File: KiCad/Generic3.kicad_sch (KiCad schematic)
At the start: 29 parts, among them J1 DC, J2 I/O, J3 USB-C, U1 ESP32-PICO-MINI-02, U2 LMR16006+FB, U3 FT231XQ

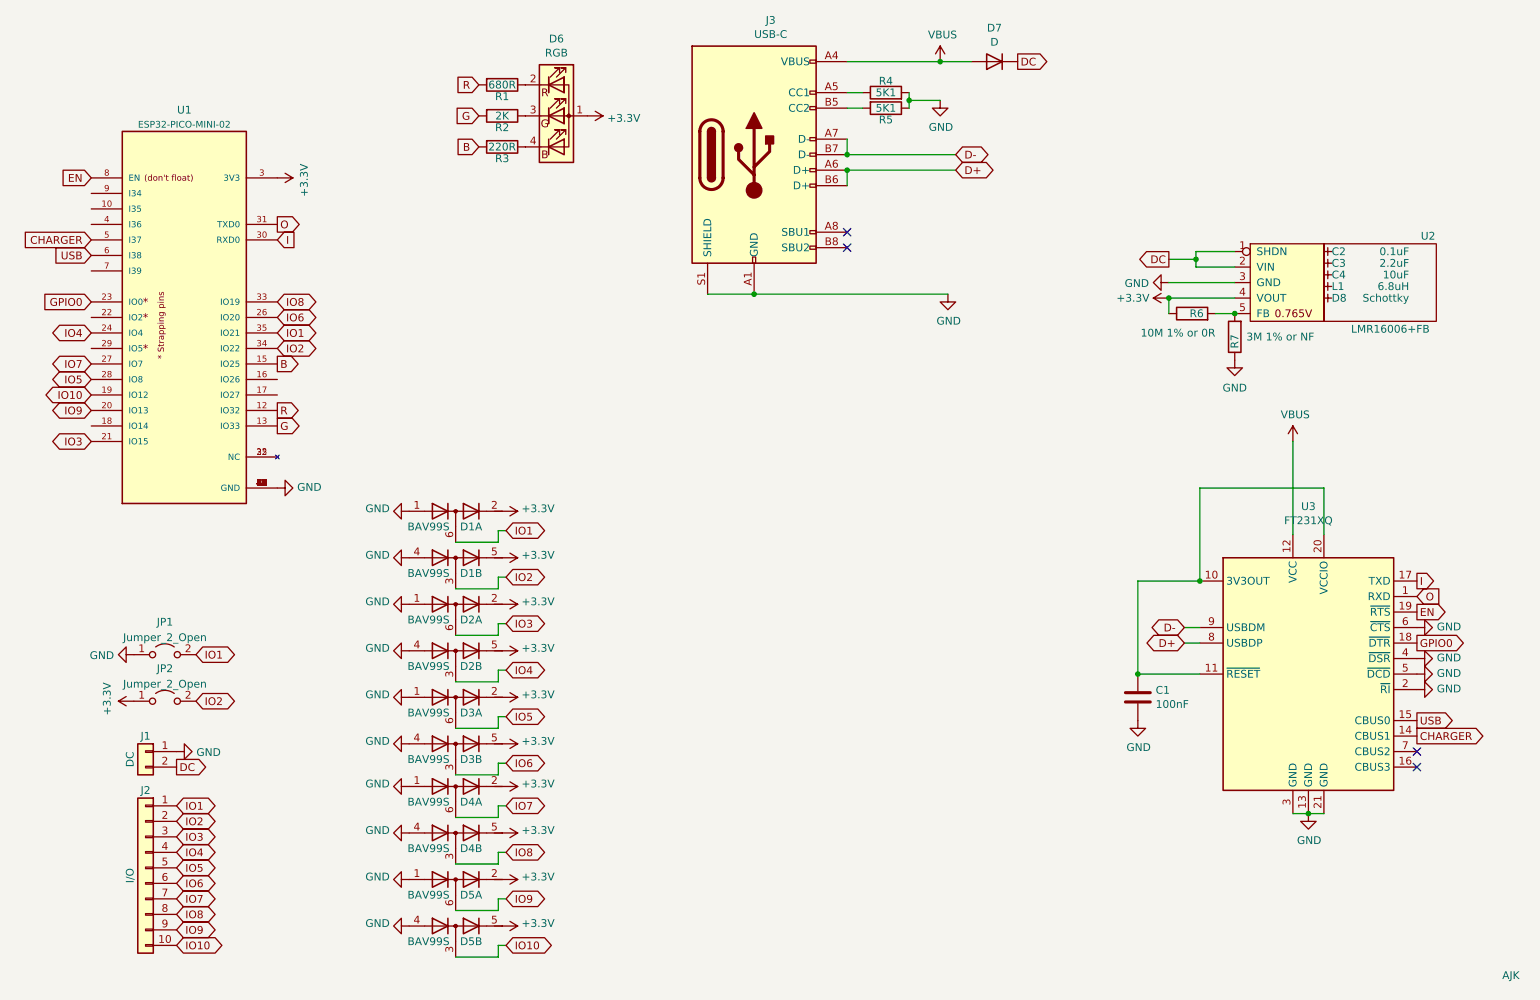
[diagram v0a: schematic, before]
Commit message: Tidy USB interface and more silkscreen
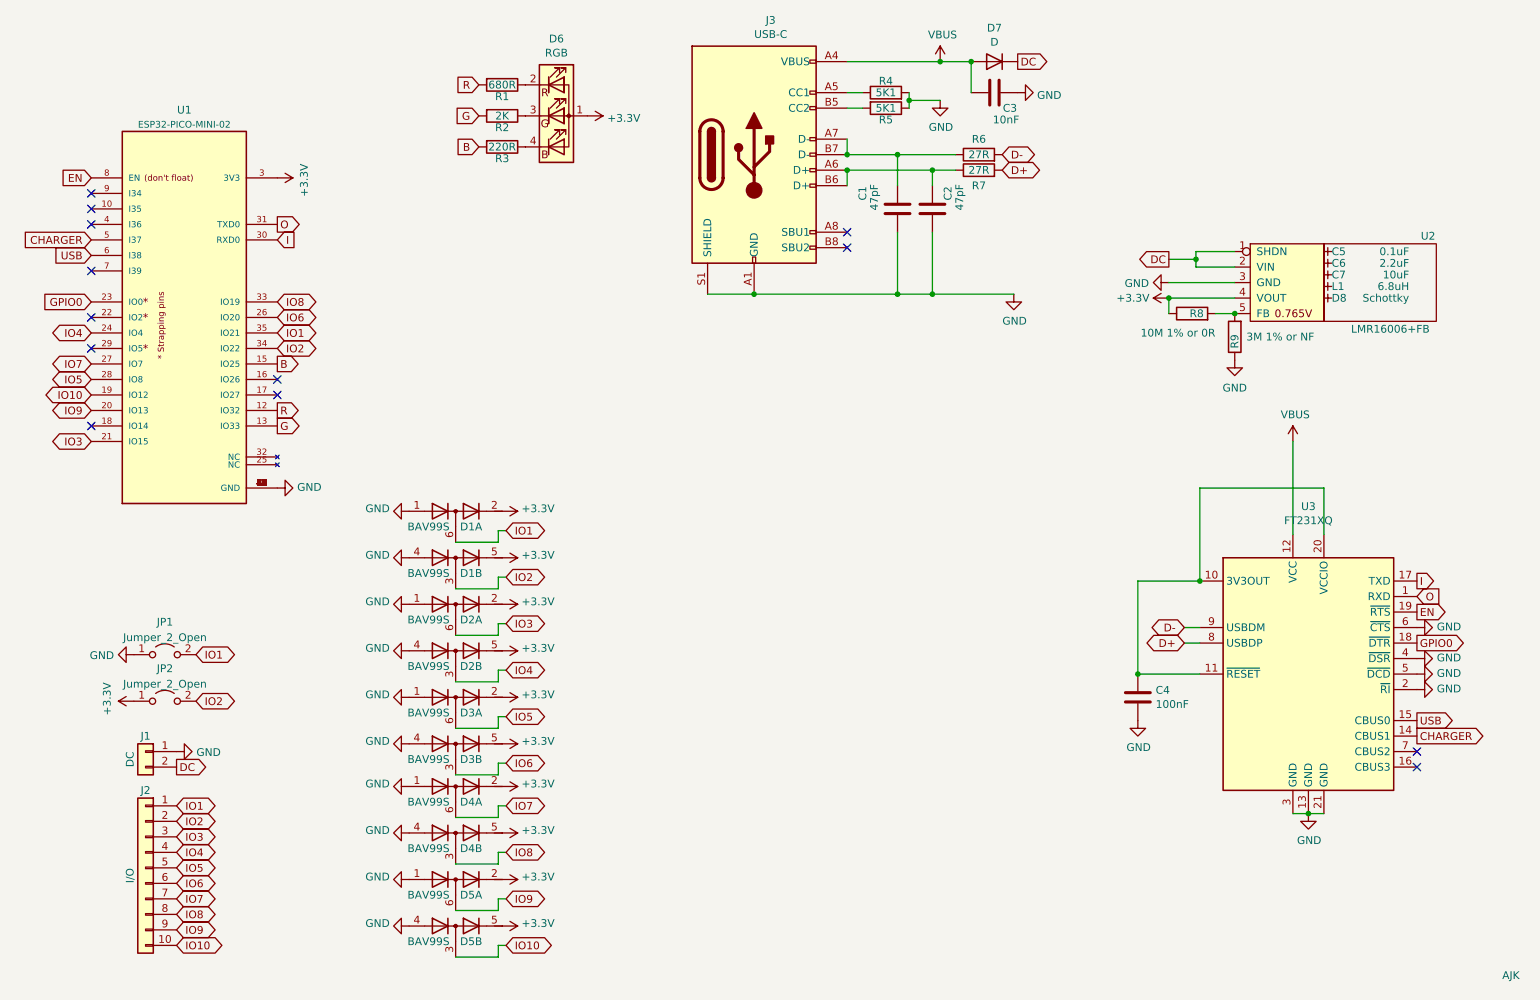
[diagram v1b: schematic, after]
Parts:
- added C1, C2: 47pF, RevK:C_0603, symbol Device:C
- added C3: 10nF, RevK:C_0603, symbol Device:C
- added R6, R7: 27R, RevK:R_0603, symbol Device:R
- renumbered C1 to C4, C2 to C5, C3 to C6, C4 to C7, R6 to R8, R7 to R9
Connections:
- net D+: now also R7.2; no longer J3.A6 (D+), J3.B6 (D+)
- net D-: now also R6.2; no longer J3.A7 (D-), J3.B7 (D-)
- net GND: now also C1.2, C2.2, C3.1
- net VBUS: now also C3.2
- net at U1.25 (NC): no longer U1.32 (NC)
- new net: C2.1, J3.A6 (D+), J3.B6 (D+), R7.1
- new net: C1.1, J3.A7 (D-), J3.B7 (D-), R6.1
- no-connect marks 4 -> 13
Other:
- title: Generic ESP32 module -> Generic ESP32-PICO-MINI module

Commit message: Logo and QR
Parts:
- added U4: QR, RevK:QR-GENERIC, symbol RevK:QR
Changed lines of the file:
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@@
     (pin "1")
+  )
+  (symbol (lib_id "RevK:QR") (at 273.685 175.26 0) (unit 1)
+    (in_bom no) (on_board yes) (fields_autoplaced)
+    (property "Reference" "U4" (id 0) (at 273.685 178.435 0)
+      (effects (font (size 1.27 1.27)) hide)
+    )
+    (property "Value" "QR" (id 1) (at 273.685 178.435 0)
+      (effects (font (size 1.27 1.27)) hide)
+    )
+    (property "Footprint" "RevK:QR-GENERIC" (id 2) (at 273.05 175.895 0)
+      (effects (font (size 1.27 1.27)) hide)
+    )
+    (property "Datasheet" "" (id 3) (at 273.05 175.895 0)
+      (effects (font (size 1.27 1.27)) hide)
+    )
+    (property "Note" "Non part, PCB printed" (id 4) (at 273.685 175.26 0)
+      (effects (font (size 1.27 1.27)) hide)
+    )
   )
   (symbol (lib_id "power:+3.3V") (at 114.3 106.68 270) (unit 1)
@@
       (reference "U3") (unit 1) (value "FT231XQ") (footprint "Package_DFN_QFN:QFN-20-1EP_4x4mm_P0.5mm_EP2.5x2.5mm")
     )
-  )
+    (path "/951ff854-9b87-48ab-8827-7adbe6fee82c"
+      (reference "U4") (unit 1) (value "QR") (footprint "RevK:QR-GENERIC")
+    )
+  )

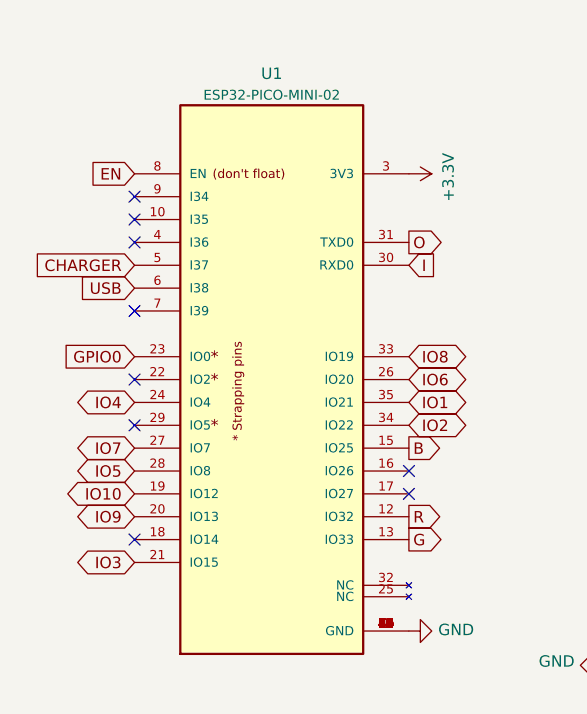
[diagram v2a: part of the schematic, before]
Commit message: Tidy GPIO usage
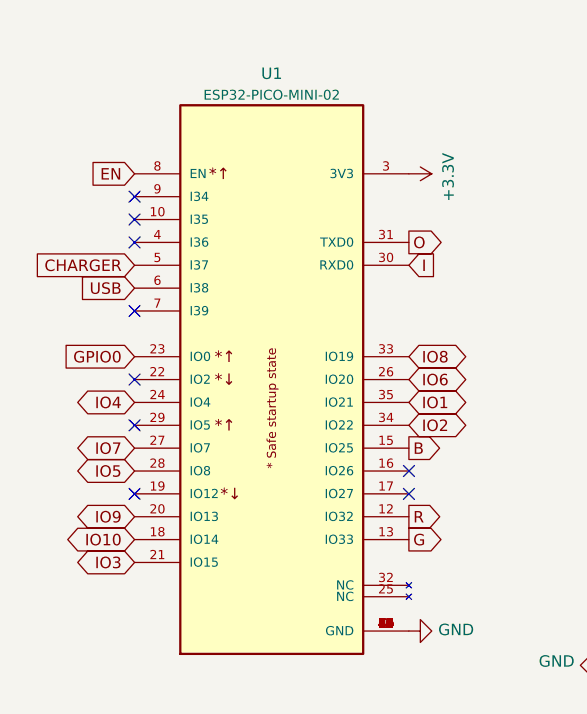
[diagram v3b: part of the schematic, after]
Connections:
- net IO10: now also U1.18 (IO14); no longer U1.19 (IO12)
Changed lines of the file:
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@@
   (no_connect (at 264.16 138.43))
   (no_connect (at 170.815 55.88))
-  (no_connect (at 46.99 85.09))
+  (no_connect (at 46.99 80.01))
   (no_connect (at 46.99 72.39))
   (no_connect (at 46.99 52.07))
@@
     )
   )
-  (global_label "IO10" (shape bidirectional) (at 46.99 80.01 180) (fields_autoplaced)
-    (effects (font (size 1.27 1.27)) (justify right))
-    (property "Intersheet References" "${INTERSHEET_REFS}" (id 0) (at 40.3115 80.0894 0)
+  (global_label "IO10" (shape bidirectional) (at 46.99 85.09 180) (fields_autoplaced)
+    (effects (font (size 1.27 1.27)) (justify right))
+    (property "Intersheet References" "${INTERSHEET_REFS}" (id 0) (at 40.3115 85.1694 0)
       (effects (font (size 1.27 1.27)) (justify right) hide)
     )

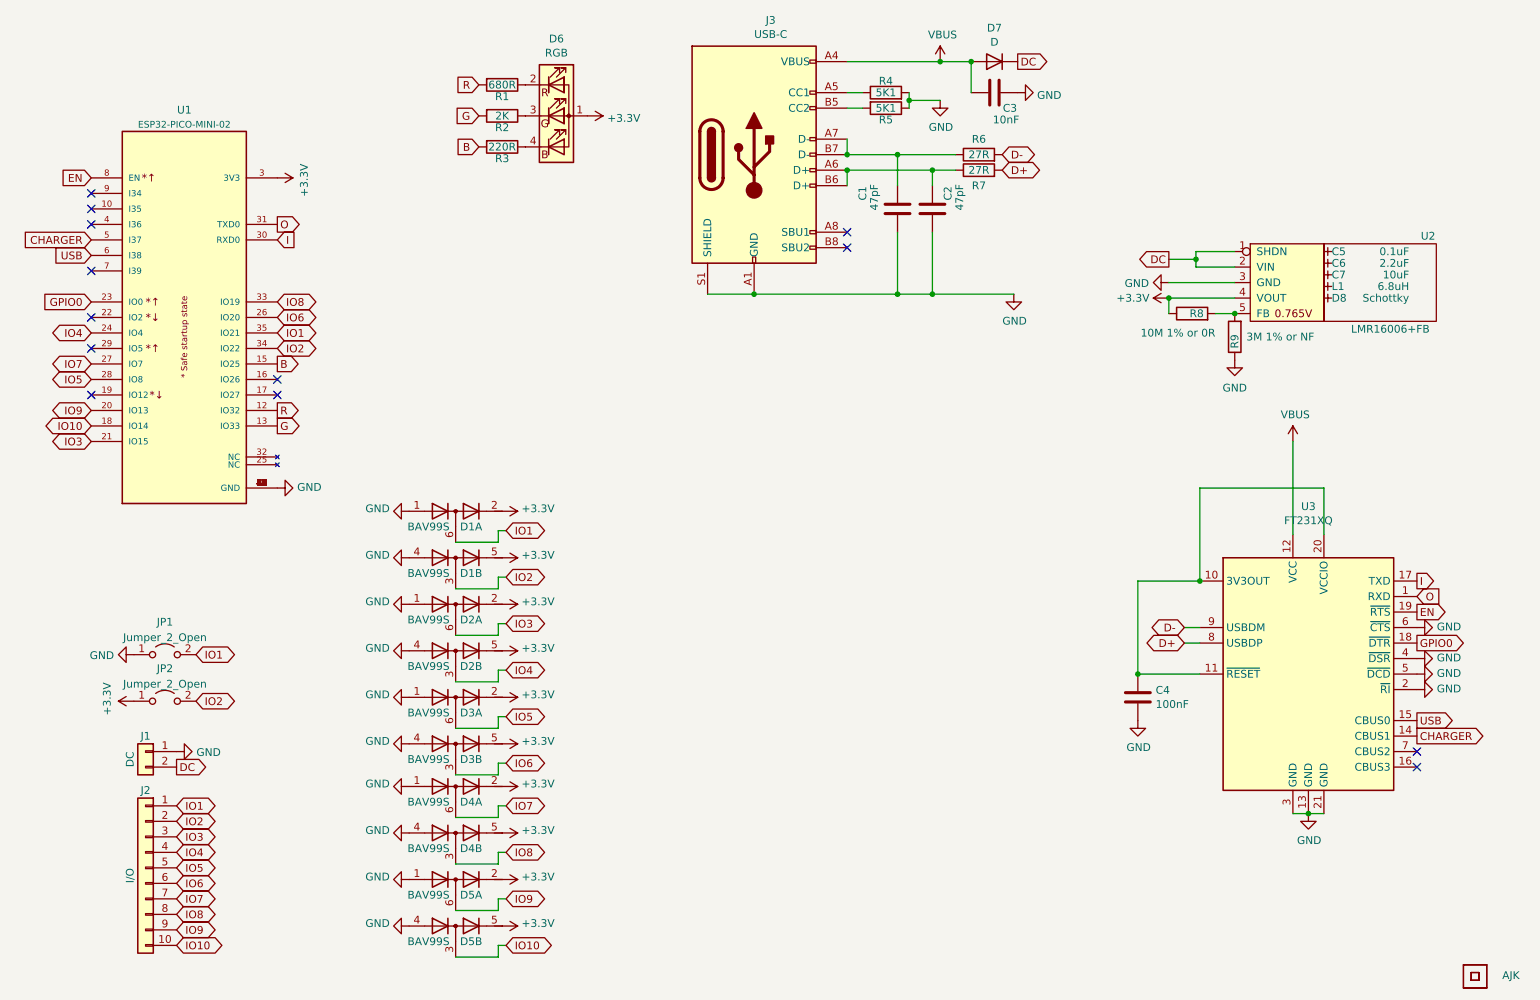
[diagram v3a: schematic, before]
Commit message: Generic3 VBUS tidy
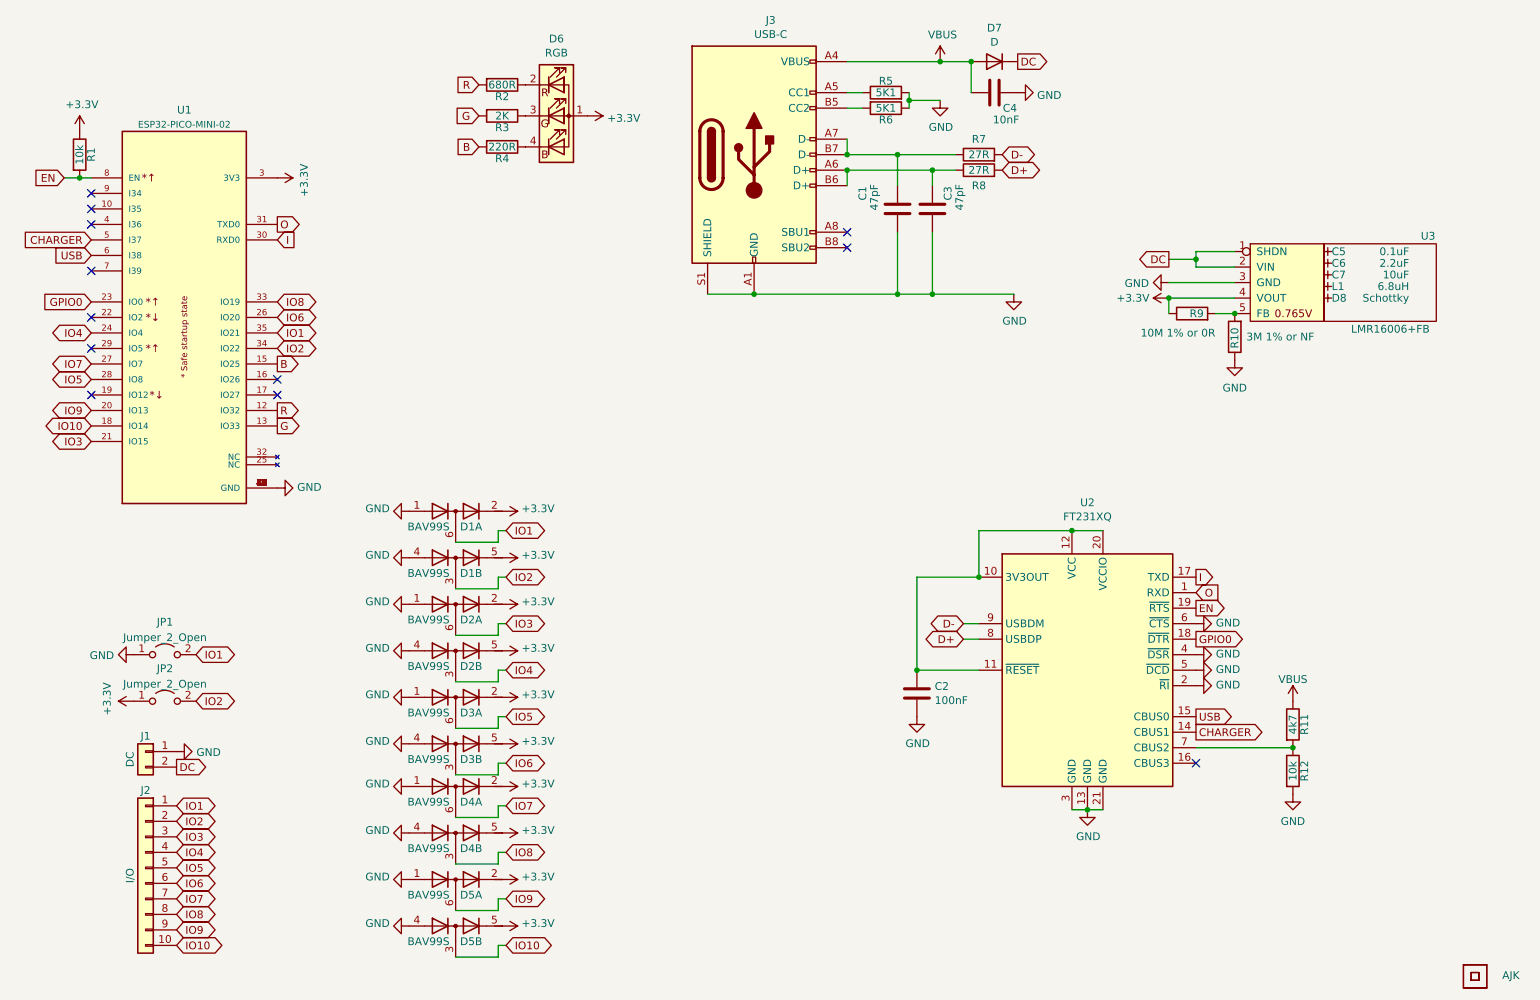
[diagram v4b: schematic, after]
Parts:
- added R1, R12: 10k, RevK:R_0603, symbol Device:R
- added R11: 4k7, RevK:R_0603, symbol Device:R
- renumbered C4 to C2, C2 to C3, C3 to C4, R9 to R10, R1 to R2, R2 to R3, R3 to R4, R4 to R5, R5 to R6, R6 to R7, R7 to R8, R8 to R9, U3 to U2, U2 to U3
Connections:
- net +3V3: now also R1.1
- net EN: now also R1.2
- net GND: now also R12.2
- net VBUS: now also R11.1; no longer U2.12 (VCC)
- net at C2.1, U2.10 (3V3OUT), U2.11 (~{RESET})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: now also U2.12 (VCC)
- net at U2.7 (CBUS2): now also R11.2, R12.1
- no-connect marks 13 -> 12
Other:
- moved on the sheet: C2, U2

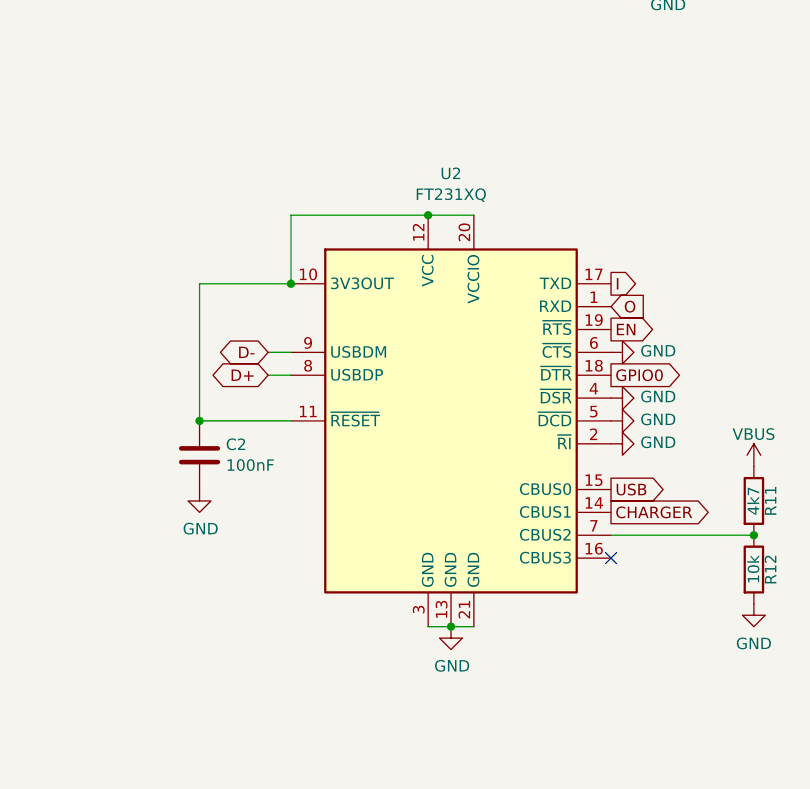
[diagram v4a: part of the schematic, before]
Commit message: Clean up GPIOs used to avoid clash with strapping at startup
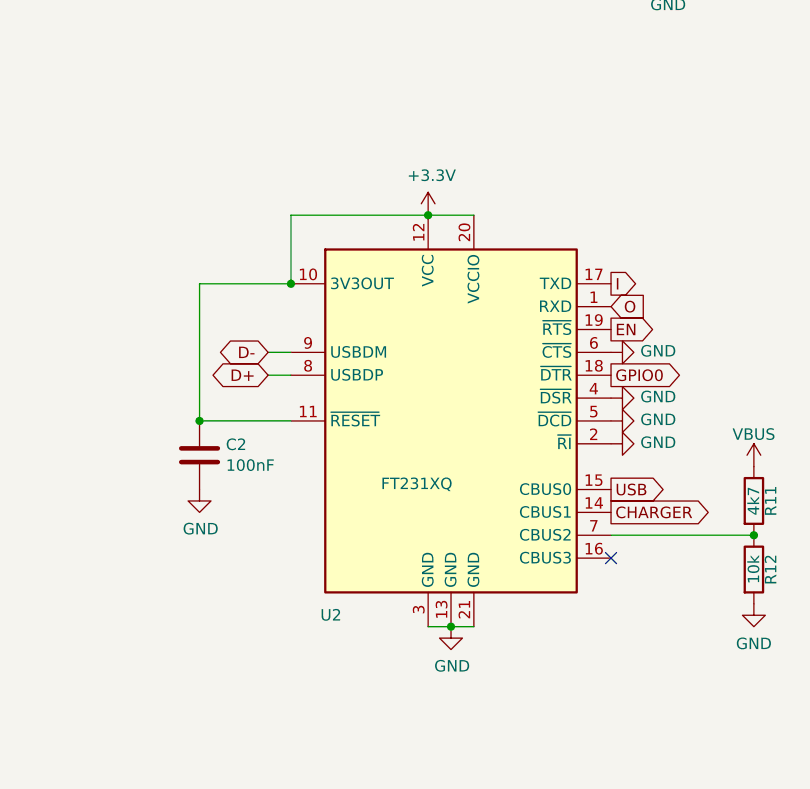
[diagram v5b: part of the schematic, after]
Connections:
- net +3V3: now also C2.1, U2.10 (3V3OUT), U2.11 (~{RESET}), U2.12 (VCC), U2.20 (VCCIO)
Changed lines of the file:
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@@
   (symbol (lib_id "Interface_USB:FT231XQ") (at 210.185 125.095 0) (unit 1)
     (in_bom yes) (on_board yes)
-    (property "Reference" "U2" (id 0) (at 210.185 97.6376 0))
-    (property "Value" "FT231XQ" (id 1) (at 210.185 99.949 0))
+    (property "Reference" "U2" (id 0) (at 196.85 146.685 0))
+    (property "Value" "FT231XQ" (id 1) (at 206.375 132.08 0))
     (property "Footprint" "Package_DFN_QFN:QFN-20-1EP_4x4mm_P0.5mm_EP2.5x2.5mm" (id 2) (at 244.475 145.415 0)
       (effects (font (size 1.27 1.27)) hide)
@@
     )
     (property "Datasheet" "" (id 3) (at 114.3 151.765 0)
+      (effects (font (size 1.27 1.27)) hide)
+    )
+    (pin "1")
+  )
+  (symbol (lib_id "power:+3.3V") (at 207.645 102.235 0) (unit 1)
+    (in_bom yes) (on_board yes)
+    (property "Reference" "#PWR0101" (id 0) (at 207.645 106.045 0)
+      (effects (font (size 1.27 1.27)) hide)
+    )
+    (property "Value" "+3.3V" (id 1) (at 208.026 97.8408 0))
+    (property "Footprint" "" (id 2) (at 207.645 102.235 0)
+      (effects (font (size 1.27 1.27)) hide)
+    )
+    (property "Datasheet" "" (id 3) (at 207.645 102.235 0)
       (effects (font (size 1.27 1.27)) hide)
     )
@@
       (reference "#PWR042") (unit 1) (value "GND") (footprint "")
     )
+    (path "/206e2d47-6ee1-4a37-ba8c-0b5ca978f401"
+      (reference "#PWR0101") (unit 1) (value "+3.3V") (footprint "")
+    )
     (path "/9c4b6535-4ff7-4315-8d63-45066a0edbfb"

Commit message: Footprint update
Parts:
- removed U2: FT231XQ, Package_DFN_QFN:QFN-20-1EP_4x4mm_P0.5mm_EP2.5x2.5mm, symbol Interface_USB:FT231XQ
- added U2: FT231XQ, RevK:QFN-20-1EP_4x4mm_P0.5mm_EP2.5x2.5mm, symbol RevK:FT231XQ
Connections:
- net +3V3: now also U2.10 (3V3OUT), U2.11 (~{RESET}), U2.12 (VCC), U2.20 (VCCIO)
- net CHARGER: now also U2.14 (CBUS1)
- net D+: now also U2.8 (USBDP)
- net D-: now also U2.9 (USBDM)
- net EN: now also U2.19 (~{RTS})
- net GND: now also U2.13 (GND), U2.2 (~{RI}), U2.21 (GND), U2.3 (GND), U2.4 (~{DSR}), U2.5 (~{DCD}), U2.6 (~{CTS}); no longer U1.54 (GND), U1.55 (GND), U1.56 (GND), U1.57 (GND), U1.58 (GND), U1.59 (GND), U1.60 (GND), U1.61 (GND)
- net GPIO0: now also U2.18 (~{DTR})
- net I: now also U2.17 (TXD)
- net O: now also U2.1 (RXD)
- net USB: now also U2.15 (CBUS0)
- net at R11.2, R12.1: now also U2.7 (CBUS2)
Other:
- moved on the sheet: C2, R11, R12
